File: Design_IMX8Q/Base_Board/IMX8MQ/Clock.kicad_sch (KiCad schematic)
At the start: 9 parts, among them U1 MIMX8MQ6CVAHZAB, Y1 25MHz, Y2 27MHz

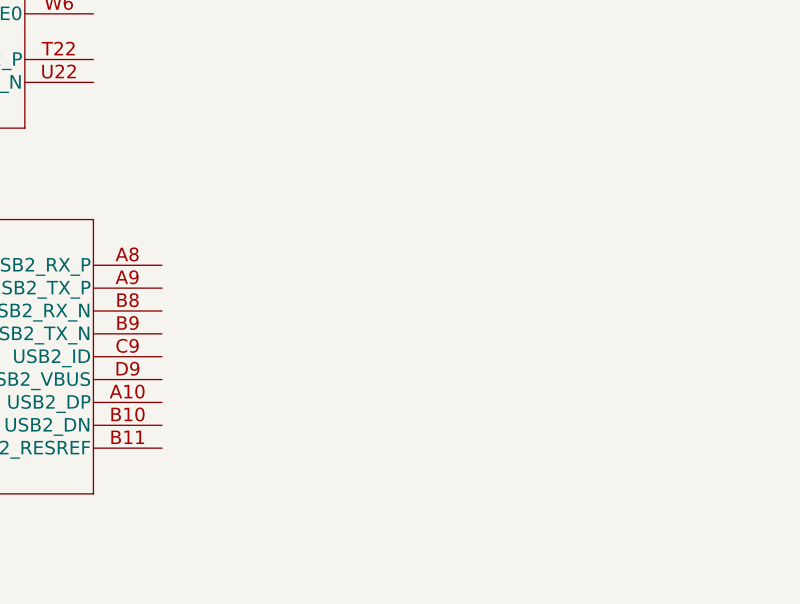
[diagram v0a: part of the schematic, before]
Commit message: changes vias pad size
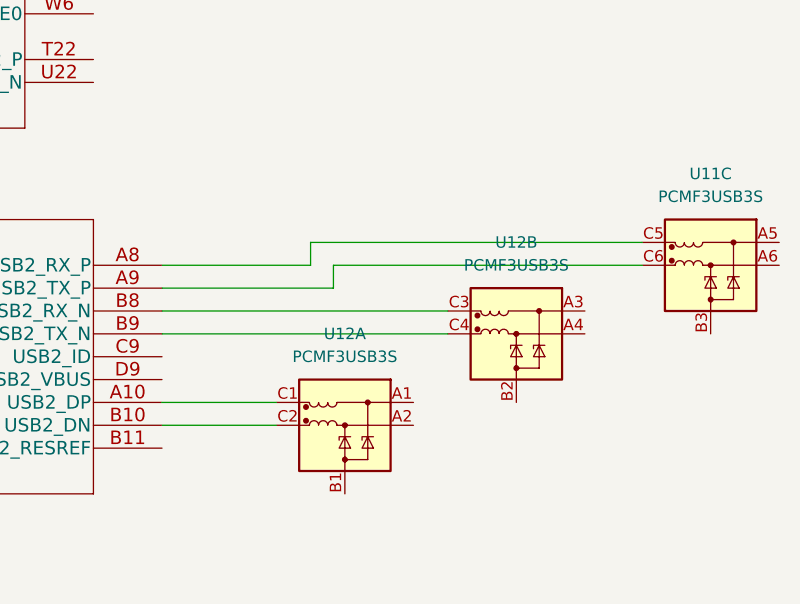
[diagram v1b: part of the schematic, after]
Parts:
- added U11, U12: PCMF3USB3S, Package_CSP:Nexperia_WLCSP-15_6-3-6_2.37x1.17mm_Layout6x3_P0.4mm, symbol Power_Protection:PCMF3USB3S
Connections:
- net at U1.A10 (USB2_DP): now also U12.C1 (CH1_OUT+)
- net at U1.A8 (USB2_RX_P): now also U11.C5 (CH3_OUT+)
- net at U1.A9 (USB2_TX_P): now also U11.C6 (CH3_OUT-)
- net at U1.B10 (USB2_DN): now also U12.C2 (CH1_OUT-)
- net at U1.B8 (USB2_RX_N): now also U12.C3 (CH2_OUT+)
- net at U1.B9 (USB2_TX_N): now also U12.C4 (CH2_OUT-)
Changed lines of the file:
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@@
+    (stroke (width 0) (type default))
+  )
+  (wire (pts (xy 157.48 91.44) (xy 189.23 91.44))
     (stroke (width 0) (type default))
   )
@@
     (stroke (width 0) (type default))
   )
+  (wire (pts (xy 157.48 88.9) (xy 189.23 88.9))
+    (stroke (width 0) (type default))
+  )
   (wire (pts (xy 72.39 90.17) (xy 72.39 92.71))
     (stroke (width 0) (type default))
@@
     (stroke (width 0) (type default))
   )
+  (wire (pts (xy 173.99 83.82) (xy 157.48 83.82))
+    (stroke (width 0) (type default))
+  )
+  (wire (pts (xy 173.99 81.28) (xy 173.99 83.82))
+    (stroke (width 0) (type default))
+  )
+  (wire (pts (xy 176.53 86.36) (xy 176.53 83.82))
+    (stroke (width 0) (type default))
+  )
   (wire (pts (xy 78.74 91.44) (xy 78.74 92.71))
     (stroke (width 0) (type default))
@@
     (stroke (width 0) (type default))
   )
+  (wire (pts (xy 157.48 86.36) (xy 176.53 86.36))
+    (stroke (width 0) (type default))
+  )
   (wire (pts (xy 66.04 92.71) (xy 72.39 92.71))
     (stroke (width 0) (type default))
@@
     (stroke (width 0) (type default))
   )
+  (wire (pts (xy 157.48 99.06) (xy 170.18 99.06))
+    (stroke (width 0) (type default))
+  )
+  (wire (pts (xy 176.53 83.82) (xy 210.82 83.82))
+    (stroke (width 0) (type default))
+  )
   (wire (pts (xy 48.26 92.71) (xy 45.72 92.71))
     (stroke (width 0) (type default))
@@
     (stroke (width 0) (type default))
   )
+  (wire (pts (xy 157.48 101.6) (xy 170.18 101.6))
+    (stroke (width 0) (type default))
+  )
   (wire (pts (xy 71.12 107.95) (xy 71.12 111.76))
     (stroke (width 0) (type default))
@@
   )
   (wire (pts (xy 91.44 88.9) (xy 78.74 88.9))
+    (stroke (width 0) (type default))
+  )
+  (wire (pts (xy 210.82 81.28) (xy 173.99 81.28))
     (stroke (width 0) (type default))
   )
@@
         (path "/980bb0ed-9dcc-491b-96e4-a3efce564505/a1d70fa9-a59c-4beb-8a9f-184aebcead08"
           (reference "#PWR015") (unit 1)
+        )
+      )
+    )
+  )
+  (symbol (lib_id "Power_Protection:PCMF3USB3S") (at 196.85 91.44 0) (mirror y) (unit 2)
+    (in_bom yes) (on_board yes) (dnp no) (fields_autoplaced)
+    (property "Reference" "U12" (at 196.85 81.28 0)
+      (effects (font (size 1.27 1.27)))
+    )
+    (property "Value" "PCMF3USB3S" (at 196.85 83.82 0)
+      (effects (font (size 1.27 1.27)))
+    )
+    (property "Footprint" "Package_CSP:Nexperia_WLCSP-15_6-3-6_2.37x1.17mm_Layout6x3_P0.4mm" (at 196.85 93.98 0)
+      (effects (font (size 1.27 1.27)) hide)
+    )
+    (property "Datasheet" "https://assets.nexperia.com/documents/data-sheet/PCMFXUSB3S_SER.pdf" (at 196.85 90.17 0)
+      (effects (font (size 1.27 1.27)) hide)
+    )
+    (pin "A1")
+    (pin "A2")
+    (pin "B1")
+    (pin "C1")
+    (pin "C2")
+    (pin "A3")
+    (pin "A4")
+    (pin "B2")
+    (pin "C3")
+    (pin "C4")
+    (pin "A5")
+    (pin "A6")
+    (pin "B3")
+    (pin "C5")
+    (pin "C6")
+    (instances
+      (project "IMX8MQ"
+        (path "/980bb0ed-9dcc-491b-96e4-a3efce564505/309a10d2-803e-4f80-ad88-886b74ec4e9b"
+          (reference "U12") (unit 2)
+        )
+        (path "/980bb0ed-9dcc-491b-96e4-a3efce564505/a1d70fa9-a59c-4beb-8a9f-184aebcead08"
+          (reference "U12") (unit 2)
         )
       )
@@
         (path "/980bb0ed-9dcc-491b-96e4-a3efce564505/a1d70fa9-a59c-4beb-8a9f-184aebcead08"
           (reference "C20") (unit 1)
+        )
+      )
+    )
+  )
+  (symbol (lib_id "Power_Protection:PCMF3USB3S") (at 177.8 101.6 0) (mirror y) (unit 1)
+    (in_bom yes) (on_board yes) (dnp no) (fields_autoplaced)
+    (property "Reference" "U12" (at 177.8 91.44 0)
+      (effects (font (size 1.27 1.27)))
+    )
+    (property "Value" "PCMF3USB3S" (at 177.8 93.98 0)
+      (effects (font (size 1.27 1.27)))
+    )
+    (property "Footprint" "Package_CSP:Nexperia_WLCSP-15_6-3-6_2.37x1.17mm_Layout6x3_P0.4mm" (at 177.8 104.14 0)
+      (effects (font (size 1.27 1.27)) hide)
+    )
+    (property "Datasheet" "https://assets.nexperia.com/documents/data-sheet/PCMFXUSB3S_SER.pdf" (at 177.8 100.33 0)
+      (effects (font (size 1.27 1.27)) hide)
+    )
+    (pin "A1")
+    (pin "A2")
+    (pin "B1")
+    (pin "C1")
+    (pin "C2")
+    (pin "A3")
+    (pin "A4")
+    (pin "B2")
+    (pin "C3")
+    (pin "C4")
+    (pin "A5")
+    (pin "A6")
+    (pin "B3")
+    (pin "C5")
+    (pin "C6")
+    (instances
+      (project "IMX8MQ"
+        (path "/980bb0ed-9dcc-491b-96e4-a3efce564505/309a10d2-803e-4f80-ad88-886b74ec4e9b"
+          (reference "U12") (unit 1)
+        )
+        (path "/980bb0ed-9dcc-491b-96e4-a3efce564505/a1d70fa9-a59c-4beb-8a9f-184aebcead08"
+          (reference "U12") (unit 1)
         )
       )
@@
         )
       )
+    )
+  )
+  (symbol (lib_id "Power_Protection:PCMF3USB3S") (at 218.44 83.82 0) (mirror y) (unit 3)
+    (in_bom yes) (on_board yes) (dnp no) (fields_autoplaced)
+    (property "Reference" "U11" (at 218.44 73.66 0)
+      (effects (font (size 1.27 1.27)))
+    )
+    (property "Value" "PCMF3USB3S" (at 218.44 76.2 0)
+      (effects (font (size 1.27 1.27)))
+    )
+    (property "Footprint" "Package_CSP:Nexperia_WLCSP-15_6-3-6_2.37x1.17mm_Layout6x3_P0.4mm" (at 218.44 86.36 0)
+      (effects (font (size 1.27 1.27)) hide)
+    )
+    (property "Datasheet" "https://assets.nexperia.com/documents/data-sheet/PCMFXUSB3S_SER.pdf" (at 218.44 82.55 0)
+      (effects (font (size 1.27 1.27)) hide)
+    )
+    (pin "A1")
+    (pin "A2")
+    (pin "B1")
+    (pin "C1")
+    (pin "C2")
+    (pin "A3")
+    (pin "A4")
+    (pin "B2")
+    (pin "C3")
+    (pin "C4")
+    (pin "A5")
+    (pin "A6")
+    (pin "B3")
+    (pin "C5")
+    (pin "C6")
+    (instances
+      (project "IMX8MQ"
+        (path "/980bb0ed-9dcc-491b-96e4-a3efce564505/309a10d2-803e-4f80-ad88-886b74ec4e9b"
+          (reference "U11") (unit 3)
+        )
+        (path "/980bb0ed-9dcc-491b-96e4-a3efce564505/a1d70fa9-a59c-4beb-8a9f-184aebcead08"
+          (reference "U11") (unit 3)
+        )
+      )

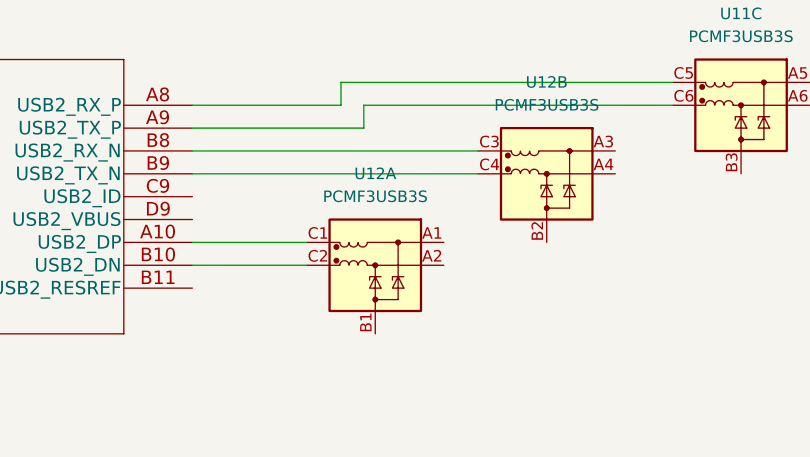
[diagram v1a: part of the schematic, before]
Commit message: Add QSPI and more color
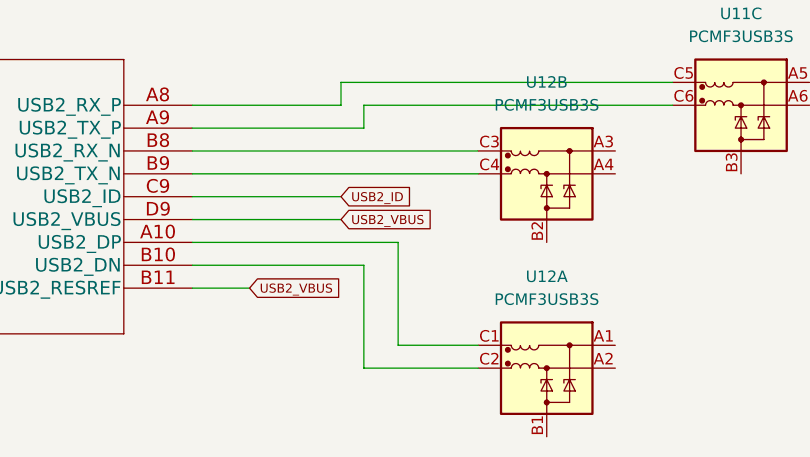
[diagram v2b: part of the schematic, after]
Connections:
- net USB2_VBUS: now reaches U1.B11 (USB2_RESREF)
- net USB2_VBUS: now also U1.D9 (USB2_VBUS)
- net USB2_ID: now reaches U1.C9 (USB2_ID)
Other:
- moved on the sheet: U12A
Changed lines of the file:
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@@
+    (stroke (width 0) (type default))
+  )
+  (wire (pts (xy 176.53 101.6) (xy 176.53 113.03))
     (stroke (width 0) (type default))
   )
@@
     (stroke (width 0) (type default))
   )
+  (wire (pts (xy 180.34 110.49) (xy 180.34 99.06))
+    (stroke (width 0) (type default))
+  )
   (wire (pts (xy 69.85 95.25) (xy 69.85 87.63))
     (stroke (width 0) (type default))
@@
     (stroke (width 0) (type default))
   )
+  (wire (pts (xy 157.48 96.52) (xy 173.99 96.52))
+    (stroke (width 0) (type default))
+  )
   (wire (pts (xy 176.53 86.36) (xy 176.53 83.82))
     (stroke (width 0) (type default))
@@
     (stroke (width 0) (type default))
   )
+  (wire (pts (xy 189.23 110.49) (xy 180.34 110.49))
+    (stroke (width 0) (type default))
+  )
   (wire (pts (xy 91.44 96.52) (xy 82.55 96.52))
     (stroke (width 0) (type default))
@@
     (stroke (width 0) (type default))
   )
-  (wire (pts (xy 157.48 99.06) (xy 170.18 99.06))
+  (wire (pts (xy 157.48 99.06) (xy 180.34 99.06))
     (stroke (width 0) (type default))
   )
@@
     (stroke (width 0) (type default))
   )
-  (wire (pts (xy 157.48 101.6) (xy 170.18 101.6))
+  (wire (pts (xy 157.48 101.6) (xy 176.53 101.6))
     (stroke (width 0) (type default))
   )
@@
     (stroke (width 0) (type default))
   )
+  (wire (pts (xy 157.48 104.14) (xy 163.83 104.14))
+    (stroke (width 0) (type default))
+  )
   (wire (pts (xy 50.8 114.3) (xy 50.8 111.76))
     (stroke (width 0) (type default))
@@
     (stroke (width 0) (type default))
   )
+  (wire (pts (xy 157.48 93.98) (xy 173.99 93.98))
+    (stroke (width 0) (type default))
+  )
   (wire (pts (xy 80.01 93.98) (xy 80.01 100.33))
     (stroke (width 0) (type default))
@@
   (wire (pts (xy 66.04 82.55) (xy 66.04 85.09))
     (stroke (width 0) (type default))
+  )
+  (wire (pts (xy 176.53 113.03) (xy 189.23 113.03))
+    (stroke (width 0) (type default))
+  )
+  (global_label "USB2_ID" (shape input) (at 173.99 93.98 0) (fields_autoplaced)
+    (effects (font (size 1 1)) (justify left))
+    (property "Intersheetrefs" "${INTERSHEET_REFS}" (at 182.4684 93.98 0)
+      (effects (font (size 1.27 1.27)) (justify left) hide)
+    )
+  )
+  (global_label "USB2_VBUS" (shape input) (at 163.83 104.14 0) (fields_autoplaced)
+    (effects (font (size 1 1)) (justify left))
+    (property "Intersheetrefs" "${INTERSHEET_REFS}" (at 174.6893 104.14 0)
+      (effects (font (size 1.27 1.27)) (justify left) hide)
+    )
+  )
+  (global_label "USB2_VBUS" (shape input) (at 173.99 96.52 0) (fields_autoplaced)
+    (effects (font (size 1 1)) (justify left))
+    (property "Intersheetrefs" "${INTERSHEET_REFS}" (at 184.8493 96.52 0)
+      (effects (font (size 1.27 1.27)) (justify left) hide)
+    )
   )
   (symbol (lib_id "power:GND") (at 45.72 85.09 0) (unit 1)
@@
     )
   )
-  (symbol (lib_id "Power_Protection:PCMF3USB3S") (at 177.8 101.6 0) (mirror y) (unit 1)
+  (symbol (lib_id "Power_Protection:PCMF3USB3S") (at 196.85 113.03 0) (mirror y) (unit 1)
     (in_bom yes) (on_board yes) (dnp no) (fields_autoplaced)
-    (property "Reference" "U12" (at 177.8 91.44 0)
-      (effects (font (size 1.27 1.27)))
-    )
-    (property "Value" "PCMF3USB3S" (at 177.8 93.98 0)
-      (effects (font (size 1.27 1.27)))
-    )
-    (property "Footprint" "Package_CSP:Nexperia_WLCSP-15_6-3-6_2.37x1.17mm_Layout6x3_P0.4mm" (at 177.8 104.14 0)
-      (effects (font (size 1.27 1.27)) hide)
-    )
-    (property "Datasheet" "https://assets.nexperia.com/documents/data-sheet/PCMFXUSB3S_SER.pdf" (at 177.8 100.33 0)
-      (effects (font (size 1.27 1.27)) hide)
-    )
+    (property "Reference" "U12" (at 196.85 102.87 0)
+      (effects (font (size 1.27 1.27)))
+    )
+    (property "Value" "PCMF3USB3S" (at 196.85 105.41 0)
+      (effects (font (size 1.27 1.27)))
+    )
+    (property "Footprint" "Package_CSP:Nexperia_WLCSP-15_6-3-6_2.37x1.17mm_Layout6x3_P0.4mm" (at 196.85 115.57 0)
+      (effects (font (size 1.27 1.27)) hide)
+    )
+    (property "Datasheet" "https://assets.nexperia.com/documents/data-sheet/PCMFXUSB3S_SER.pdf" (at 196.85 111.76 0)
+      (effects (font (size 1.27 1.27)) hide)
+    )

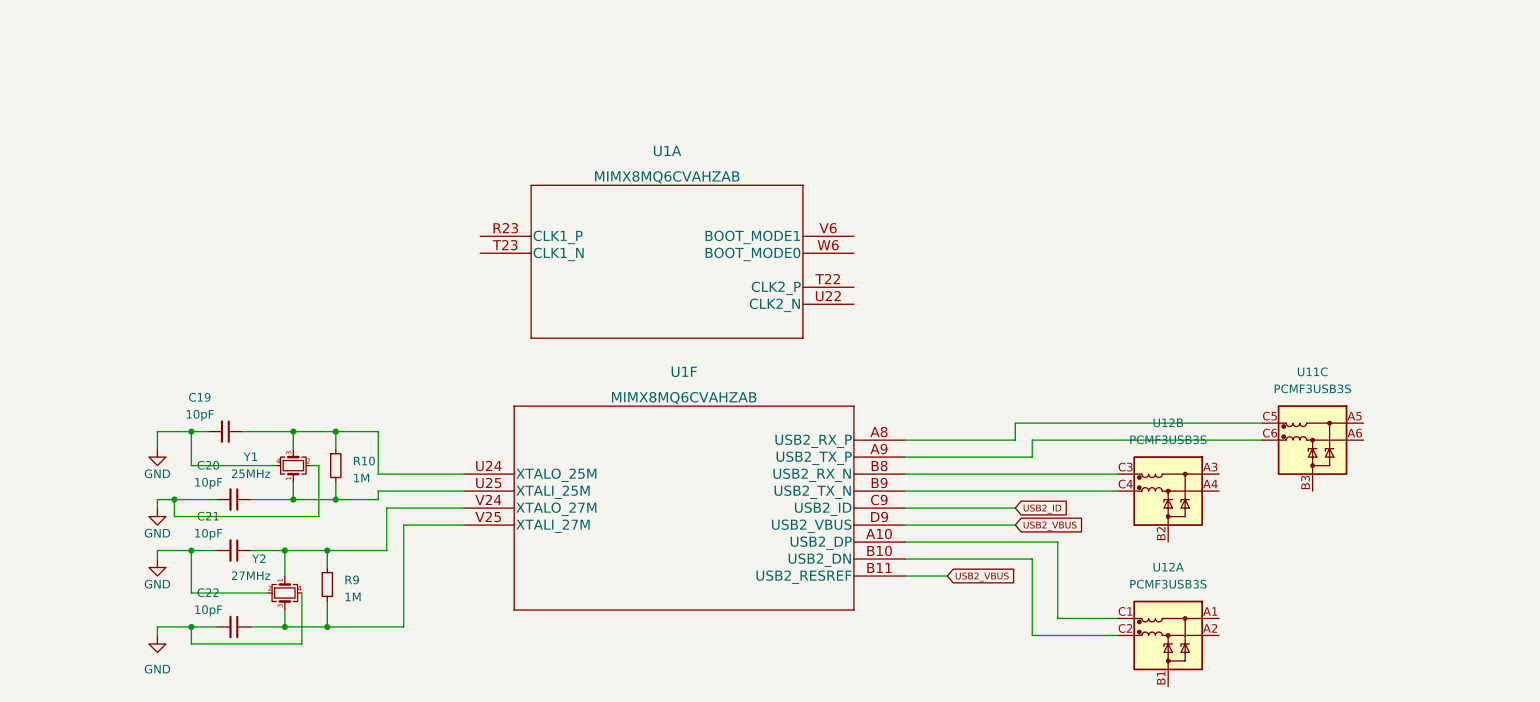
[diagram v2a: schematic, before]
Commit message: it was inserted power control system
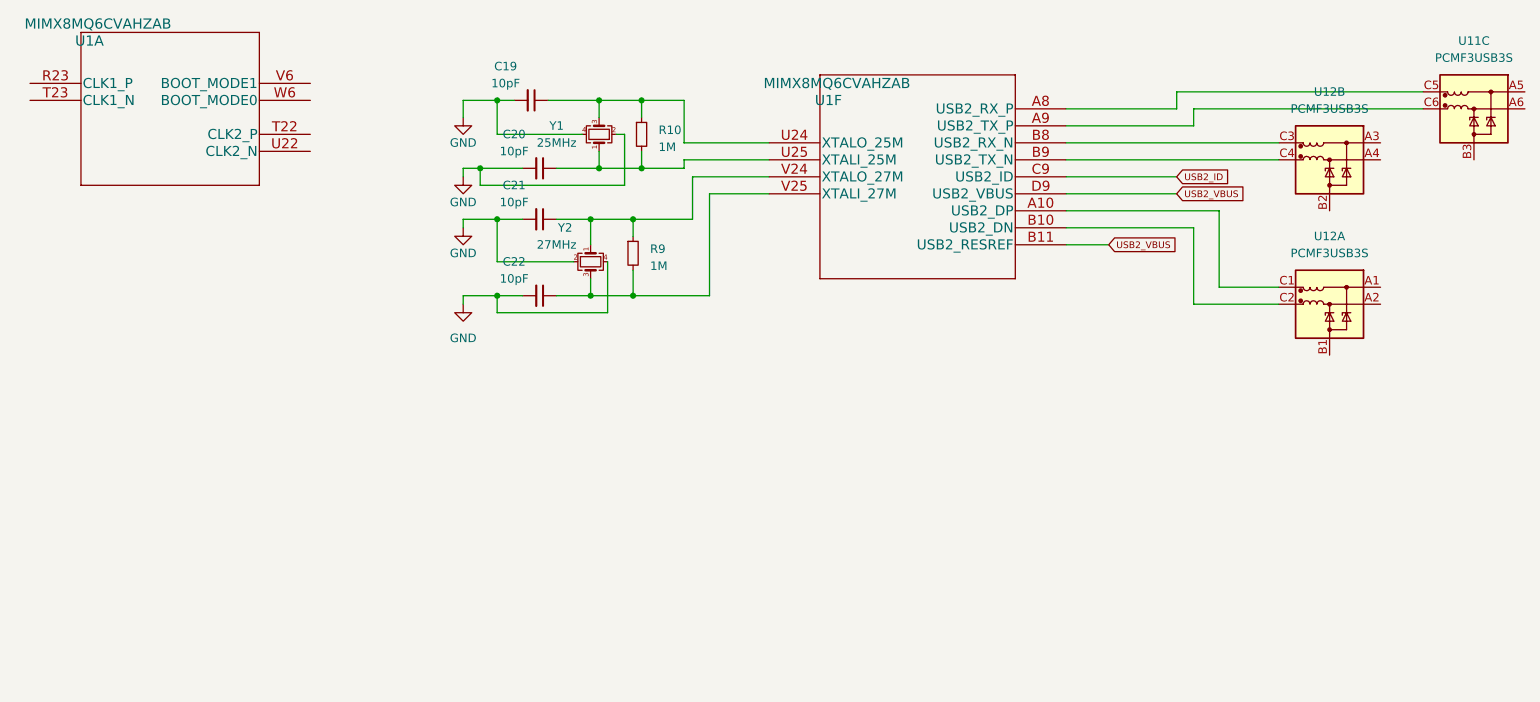
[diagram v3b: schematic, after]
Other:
- moved on the sheet: C19, C20, C21, C22, R10, R9, U11C, U12A, U12B, U1A, U1F, Y1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
